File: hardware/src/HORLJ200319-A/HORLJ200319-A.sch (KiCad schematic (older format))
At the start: 0 parts

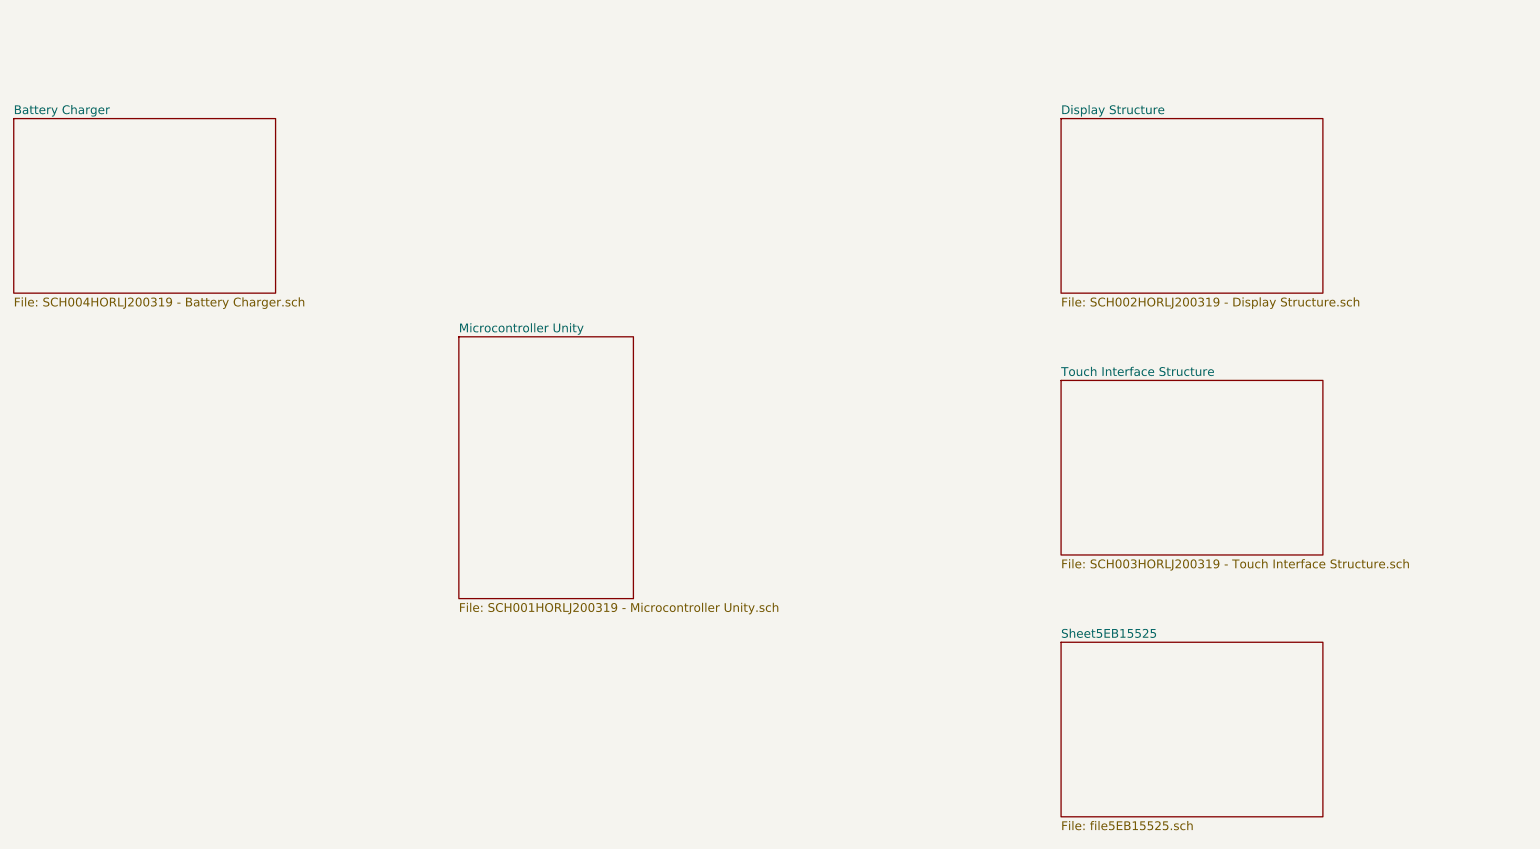
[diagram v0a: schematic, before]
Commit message: Insere MockUps digitais e inicia o projeto da PCB.
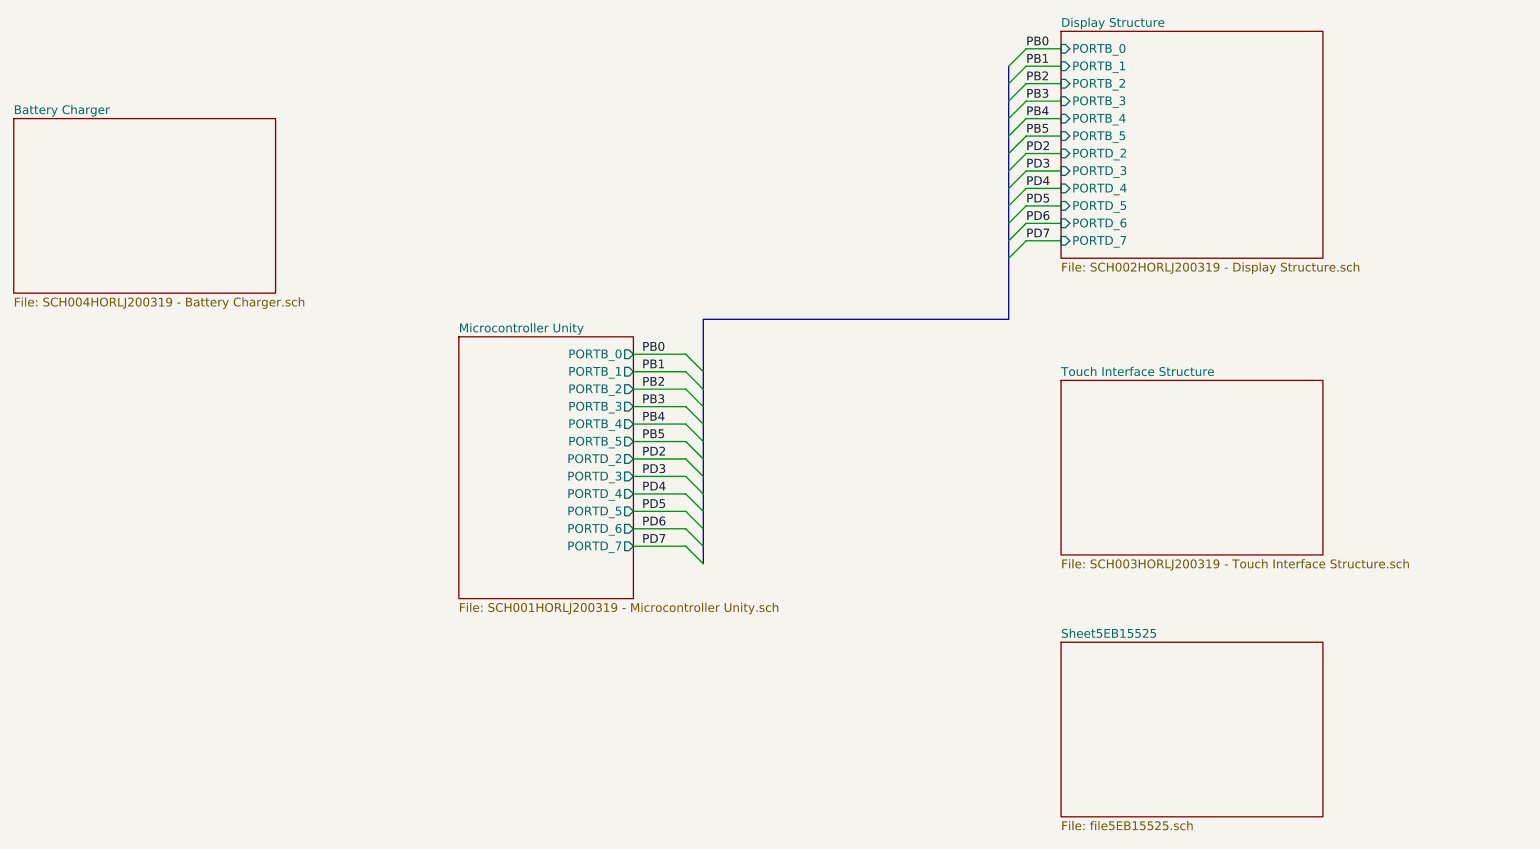
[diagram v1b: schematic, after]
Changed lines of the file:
@@
 F0 "Microcontroller Unity" 50
 F1 "SCH001HORLJ200319 - Microcontroller Unity.sch" 50
-$EndSheet
-$Sheet
-S 7500 1500 1500 1000
+F2 "PORTB_0" O R 5050 2850 50
+F3 "PORTB_1" O R 5050 2950 50
+F4 "PORTB_2" O R 5050 3050 50
+F5 "PORTB_3" O R 5050 3150 50
+F6 "PORTB_4" O R 5050 3250 50
+F7 "PORTB_5" O R 5050 3350 50
+F8 "PORTD_2" O R 5050 3450 50
+F9 "PORTD_3" O R 5050 3550 50
+F10 "PORTD_4" O R 5050 3650 50
+F11 "PORTD_5" O R 5050 3750 50
+F12 "PORTD_6" O R 5050 3850 50
+F13 "PORTD_7" O R 5050 3950 50
+$EndSheet
+$Sheet
+S 7500 1000 1500 1300
 U 5E79D498
 F0 "Display Structure" 50
 F1 "SCH002HORLJ200319 - Display Structure.sch" 50
+F2 "PORTB_0" I L 7500 1100 50
+F3 "PORTB_1" I L 7500 1200 50
+F4 "PORTB_2" I L 7500 1300 50
+F5 "PORTB_3" I L 7500 1400 50
+F6 "PORTB_4" I L 7500 1500 50
+F7 "PORTB_5" I L 7500 1600 50
+F8 "PORTD_2" I L 7500 1700 50
+F9 "PORTD_3" I L 7500 1800 50
+F10 "PORTD_4" I L 7500 1900 50
+F11 "PORTD_5" I L 7500 2000 50
+F12 "PORTD_6" I L 7500 2100 50
+F13 "PORTD_7" I L 7500 2200 50
 $EndSheet
 $Sheet
@@
 F1 "file5EB15525.sch" 50
 $EndSheet
+Wire Wire Line
+	5350 2850 5050 2850
+Wire Wire Line
+	5350 2950 5050 2950
+Wire Wire Line
+	5050 3050 5350 3050
+Wire Wire Line
+	5350 3150 5050 3150
+Wire Wire Line
+	5350 3250 5050 3250
+Wire Wire Line
+	5350 3350 5050 3350
+Wire Wire Line
+	5350 3450 5050 3450
+Wire Wire Line
+	5350 3550 5050 3550
+Wire Wire Line
+	5350 3650 5050 3650
+Wire Wire Line
+	5350 3750 5050 3750
+Wire Wire Line
+	5350 3850 5050 3850
+Wire Wire Line
+	5050 3950 5350 3950
+Entry Wire Line
+	5350 3050 5450 3150
+Entry Wire Line
+	5350 3150 5450 3250
+Entry Wire Line
+	5350 3250 5450 3350
+Entry Wire Line
+	5350 3350 5450 3450
+Entry Wire Line
+	5350 3450 5450 3550
+Entry Wire Line
+	5350 3550 5450 3650
+Entry Wire Line
+	5350 3650 5450 3750
+Entry Wire Line
+	5350 3750 5450 3850
+Entry Wire Line
+	5350 3850 5450 3950
+Entry Wire Line
+	5350 3950 5450 4050
+Entry Wire Line
+	5350 2950 5450 3050
+Entry Wire Line
+	5350 2850 5450 2950
+Entry Wire Line
+	7300 1100 7200 1200
+Wire Wire Line
+	7500 1100 7300 1100
+Entry Wire Line
+	7300 1200 7200 1300
+Wire Wire Line
+	7500 1200 7300 1200
+Entry Wire Line
+	7300 1300 7200 1400
+Wire Wire Line
+	7500 1300 7300 1300
+Entry Wire Line
+	7300 1400 7200 1500
+Wire Wire Line
+	7500 1400 7300 1400
+Entry Wire Line
+	7300 1500 7200 1600
+Wire Wire Line
+	7500 1500 7300 1500
+Entry Wire Line
+	7300 1600 7200 1700
+Wire Wire Line
+	7500 1600 7300 1600
+Entry Wire Line
+	7300 1700 7200 1800
+Wire Wire Line
+	7500 1700 7300 1700
+Entry Wire Line
+	7300 1800 7200 1900
+Wire Wire Line
+	7500 1800 7300 1800
+Entry Wire Line
+	7300 1900 7200 2000
+Entry Wire Line
+	7300 2000 7200 2100
+Wire Wire Line
+	7500 2000 7300 2000
+Entry Wire Line
+	7300 2100 7200 2200
+Wire Wire Line
+	7500 2100 7300 2100
+Entry Wire Line
+	7300 2200 7200 2300
+Wire Wire Line
+	7500 2200 7300 2200
+Wire Wire Line
+	7300 1900 7500 1900
+Wire Bus Line
+	5450 2650 7200 2650
+Text Label 5100 2850 0    50   ~ 0
+PB0
+Text Label 5100 2950 0    50   ~ 0
+PB1
+Text Label 5100 3050 0    50   ~ 0
+PB2
+Text Label 5100 3150 0    50   ~ 0
+PB3
+Text Label 5100 3250 0    50   ~ 0
+PB4
+Text Label 5100 3350 0    50   ~ 0
+PB5
+Text Label 5100 3450 0    50   ~ 0
+PD2
+Text Label 5100 3550 0    50   ~ 0
+PD3
+Text Label 5100 3650 0    50   ~ 0
+PD4
+Text Label 5100 3750 0    50   ~ 0
+PD5
+Text Label 5100 3850 0    50   ~ 0
+PD6
+Text Label 5100 3950 0    50   ~ 0
+PD7
+Text Label 7300 1100 0    50   ~ 0
+PB0
+Text Label 7300 1200 0    50   ~ 0
+PB1
+Text Label 7300 1300 0    50   ~ 0
+PB2
+Text Label 7300 1400 0    50   ~ 0
+PB3
+Text Label 7300 1500 0    50   ~ 0
+PB4
+Text Label 7300 1600 0    50   ~ 0
+PB5
+Text Label 7300 1700 0    50   ~ 0
+PD2
+Text Label 7300 1800 0    50   ~ 0
+PD3
+Text Label 7300 1900 0    50   ~ 0
+PD4
+Text Label 7300 2000 0    50   ~ 0
+PD5
+Wire Bus Line
+	5450 2650 5450 4050
+Wire Bus Line
+	7200 1200 7200 2650
+Text Label 7300 2100 0    50   ~ 0
+PD6
+Text Label 7300 2200 0    50   ~ 0
+PD7
 $EndSCHEMATC

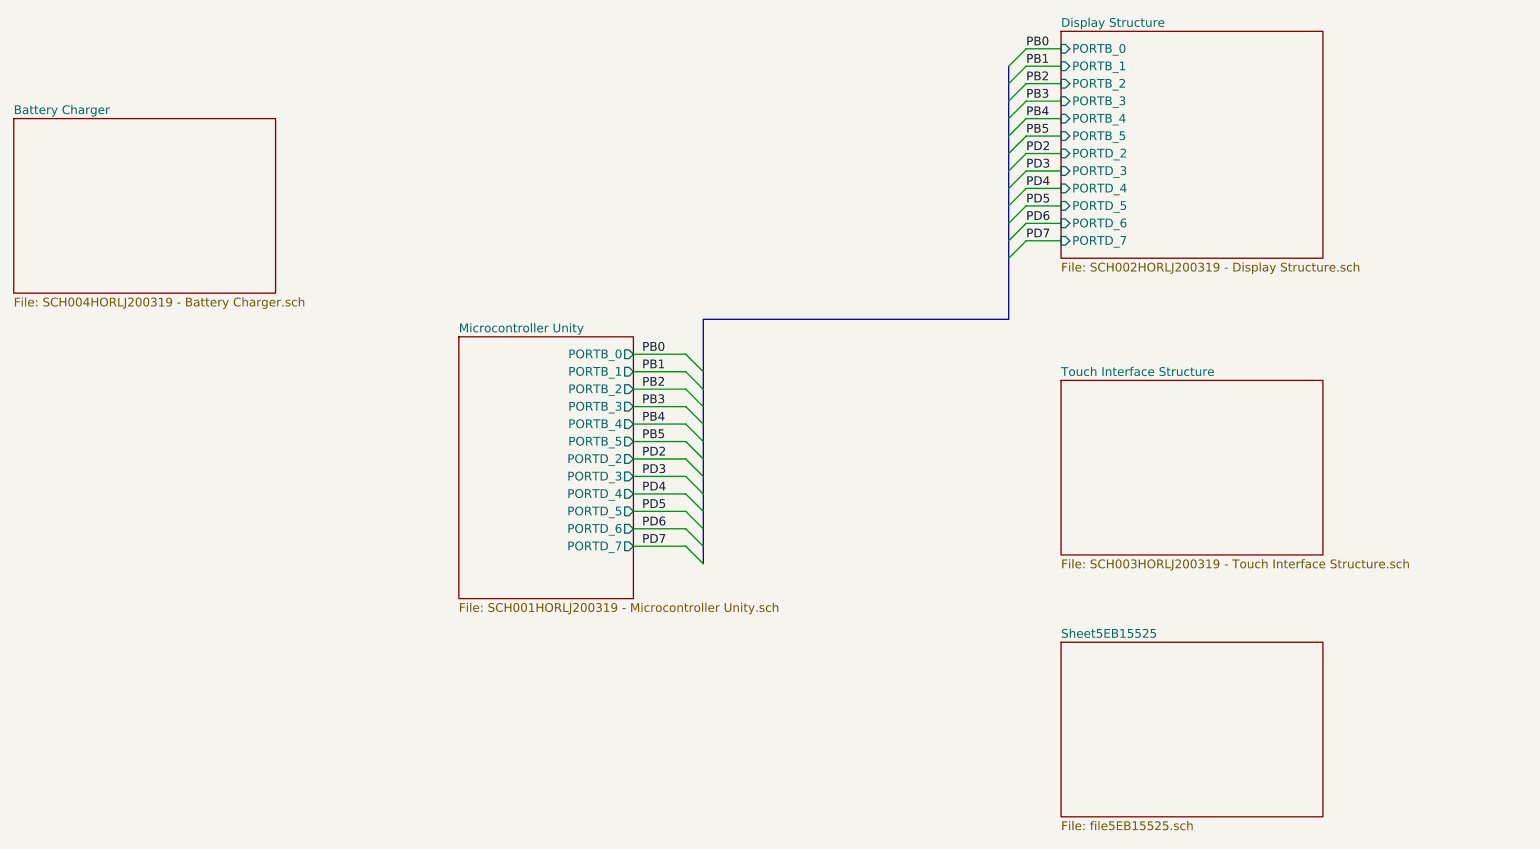
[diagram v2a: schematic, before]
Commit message: Atualiza o pinout do microcontrolador. Implementa arquivo de simulação do hardware.
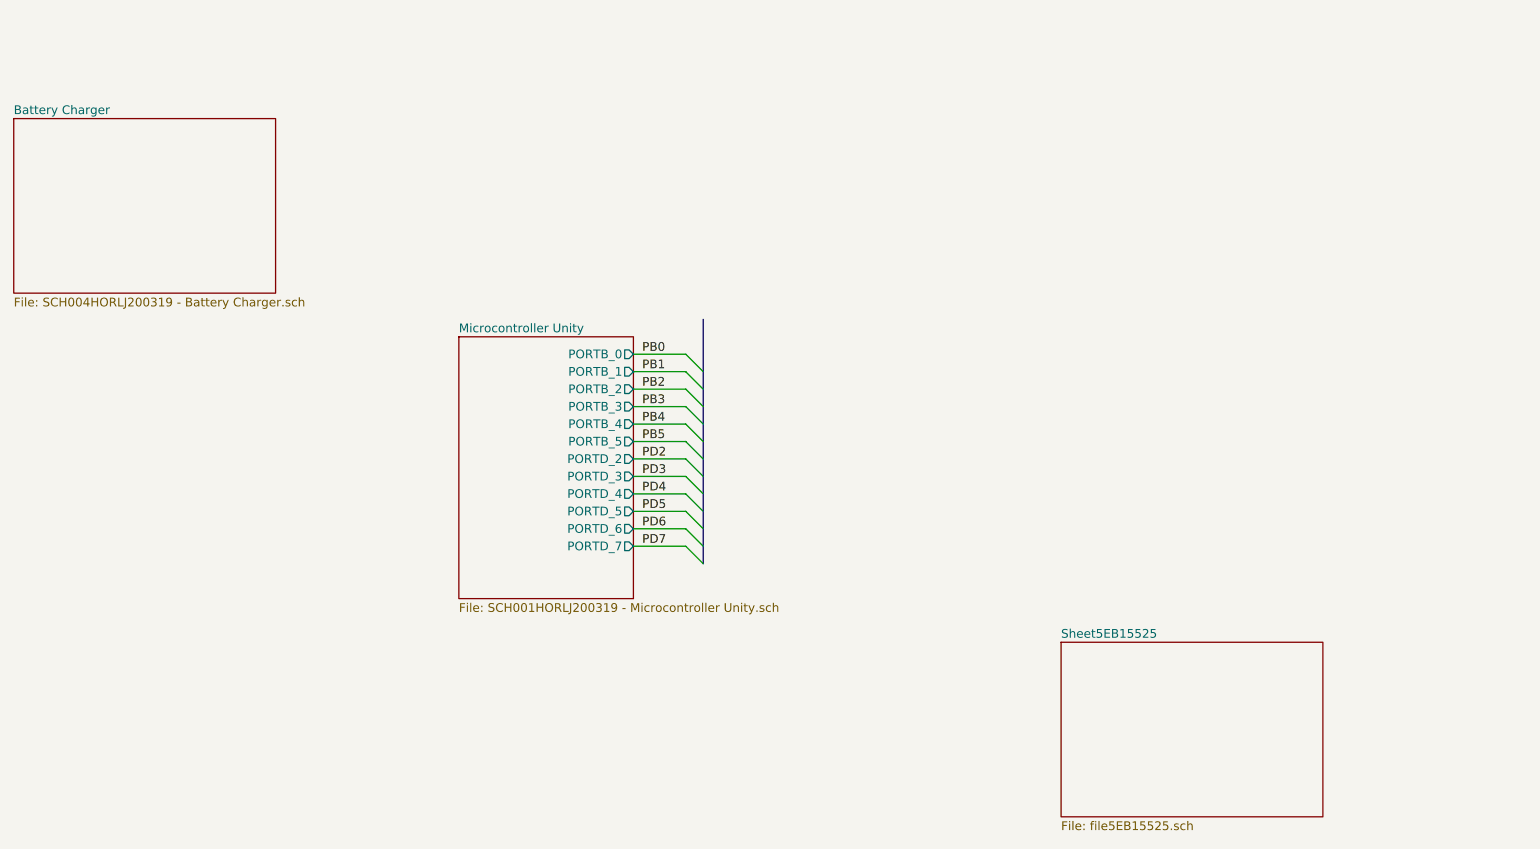
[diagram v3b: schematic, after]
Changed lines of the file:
@@
 $Descr A4 11693 8268
 encoding utf-8
-Sheet 1 10
+Sheet 1 4
 Title ""
 Date ""
@@
 Comment4 ""
 $EndDescr
-$Sheet
-S 4050 2750 1000 1500
-U 5E76982B
-F0 "Microcontroller Unity" 50
-F1 "SCH001HORLJ200319 - Microcontroller Unity.sch" 50
-F2 "PORTB_0" O R 5050 2850 50
-F3 "PORTB_1" O R 5050 2950 50
-F4 "PORTB_2" O R 5050 3050 50
-F5 "PORTB_3" O R 5050 3150 50
-F6 "PORTB_4" O R 5050 3250 50
-F7 "PORTB_5" O R 5050 3350 50
-F8 "PORTD_2" O R 5050 3450 50
-F9 "PORTD_3" O R 5050 3550 50
-F10 "PORTD_4" O R 5050 3650 50
-F11 "PORTD_5" O R 5050 3750 50
-F12 "PORTD_6" O R 5050 3850 50
-F13 "PORTD_7" O R 5050 3950 50
-$EndSheet
-$Sheet
-S 7500 1000 1500 1300
-U 5E79D498
-F0 "Display Structure" 50
-F1 "SCH002HORLJ200319 - Display Structure.sch" 50
-F2 "PORTB_0" I L 7500 1100 50
-F3 "PORTB_1" I L 7500 1200 50
-F4 "PORTB_2" I L 7500 1300 50
-F5 "PORTB_3" I L 7500 1400 50
-F6 "PORTB_4" I L 7500 1500 50
-F7 "PORTB_5" I L 7500 1600 50
-F8 "PORTD_2" I L 7500 1700 50
-F9 "PORTD_3" I L 7500 1800 50
-F10 "PORTD_4" I L 7500 1900 50
-F11 "PORTD_5" I L 7500 2000 50
-F12 "PORTD_6" I L 7500 2100 50
-F13 "PORTD_7" I L 7500 2200 50
-$EndSheet
-$Sheet
-S 7500 3000 1500 1000
-U 5E7AB605
-F0 "Touch Interface Structure" 50
-F1 "SCH003HORLJ200319 - Touch Interface Structure.sch" 50
-$EndSheet
 $Sheet
 S 1500 1500 1500 1000
@@
 Wire Wire Line
 	5050 3950 5350 3950
-Entry Wire Line
-	5350 3050 5450 3150
-Entry Wire Line
-	5350 3150 5450 3250
-Entry Wire Line
-	5350 3250 5450 3350
-Entry Wire Line
-	5350 3350 5450 3450
-Entry Wire Line
-	5350 3450 5450 3550
-Entry Wire Line
-	5350 3550 5450 3650
-Entry Wire Line
-	5350 3650 5450 3750
-Entry Wire Line
-	5350 3750 5450 3850
-Entry Wire Line
-	5350 3850 5450 3950
-Entry Wire Line
-	5350 3950 5450 4050
-Entry Wire Line
-	5350 2950 5450 3050
-Entry Wire Line
-	5350 2850 5450 2950
-Entry Wire Line
-	7300 1100 7200 1200
-Wire Wire Line
-	7500 1100 7300 1100
-Entry Wire Line
-	7300 1200 7200 1300
-Wire Wire Line
-	7500 1200 7300 1200
-Entry Wire Line
-	7300 1300 7200 1400
-Wire Wire Line
-	7500 1300 7300 1300
-Entry Wire Line
-	7300 1400 7200 1500
-Wire Wire Line
-	7500 1400 7300 1400
-Entry Wire Line
-	7300 1500 7200 1600
-Wire Wire Line
-	7500 1500 7300 1500
-Entry Wire Line
-	7300 1600 7200 1700
-Wire Wire Line
-	7500 1600 7300 1600
-Entry Wire Line
-	7300 1700 7200 1800
-Wire Wire Line
-	7500 1700 7300 1700
-Entry Wire Line
-	7300 1800 7200 1900
-Wire Wire Line
-	7500 1800 7300 1800
-Entry Wire Line
-	7300 1900 7200 2000
-Entry Wire Line
-	7300 2000 7200 2100
-Wire Wire Line
-	7500 2000 7300 2000
-Entry Wire Line
-	7300 2100 7200 2200
-Wire Wire Line
-	7500 2100 7300 2100
-Entry Wire Line
-	7300 2200 7200 2300
-Wire Wire Line
-	7500 2200 7300 2200
-Wire Wire Line
-	7300 1900 7500 1900
-Wire Bus Line
-	5450 2650 7200 2650
 Text Label 5100 2850 0    50   ~ 0
 PB0
@@
 Text Label 5100 3950 0    50   ~ 0
 PD7
-Text Label 7300 1100 0    50   ~ 0
-PB0
-Text Label 7300 1200 0    50   ~ 0
-PB1
-Text Label 7300 1300 0    50   ~ 0
-PB2
-Text Label 7300 1400 0    50   ~ 0
-PB3
-Text Label 7300 1500 0    50   ~ 0
-PB4
-Text Label 7300 1600 0    50   ~ 0
-PB5
-Text Label 7300 1700 0    50   ~ 0
-PD2
-Text Label 7300 1800 0    50   ~ 0
-PD3
-Text Label 7300 1900 0    50   ~ 0
-PD4
-Text Label 7300 2000 0    50   ~ 0
-PD5
-Text Label 7300 2100 0    50   ~ 0
-PD6
-Text Label 7300 2200 0    50   ~ 0
-PD7
 Wire Bus Line
 	5450 2650 5450 4050
-Wire Bus Line
-	7200 1200 7200 2650
+Entry Wire Line
+	5350 2850 5450 2950
+Entry Wire Line
+	5350 2950 5450 3050
+Entry Wire Line
+	5350 3950 5450 4050
+Entry Wire Line
+	5350 3850 5450 3950
+Entry Wire Line
+	5350 3750 5450 3850
+Entry Wire Line
+	5350 3650 5450 3750
+Entry Wire Line
+	5350 3550 5450 3650
+Entry Wire Line
+	5350 3450 5450 3550
+Entry Wire Line
+	5350 3350 5450 3450
+Entry Wire Line
+	5350 3250 5450 3350
+Entry Wire Line
+	5350 3150 5450 3250
+Entry Wire Line
+	5350 3050 5450 3150
+$Sheet
+S 4050 2750 1000 1500
+U 5E76982B
+F0 "Microcontroller Unity" 50
+F1 "SCH001HORLJ200319 - Microcontroller Unity.sch" 50
+F2 "PORTB_0" O R 5050 2850 50
+F3 "PORTB_1" O R 5050 2950 50
+F4 "PORTB_2" O R 5050 3050 50
+F5 "PORTB_3" O R 5050 3150 50
+F6 "PORTB_4" O R 5050 3250 50
+F7 "PORTB_5" O R 5050 3350 50
+F8 "PORTD_2" O R 5050 3450 50
+F9 "PORTD_3" O R 5050 3550 50
+F10 "PORTD_4" O R 5050 3650 50
+F11 "PORTD_5" O R 5050 3750 50
+F12 "PORTD_6" O R 5050 3850 50
+F13 "PORTD_7" O R 5050 3950 50
+$EndSheet
 $EndSCHEMATC
